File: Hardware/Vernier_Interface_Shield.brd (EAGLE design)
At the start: 91.4 x 71.1 mm, 37 parts, among them U1 74HC4052SO, U2 LMV358

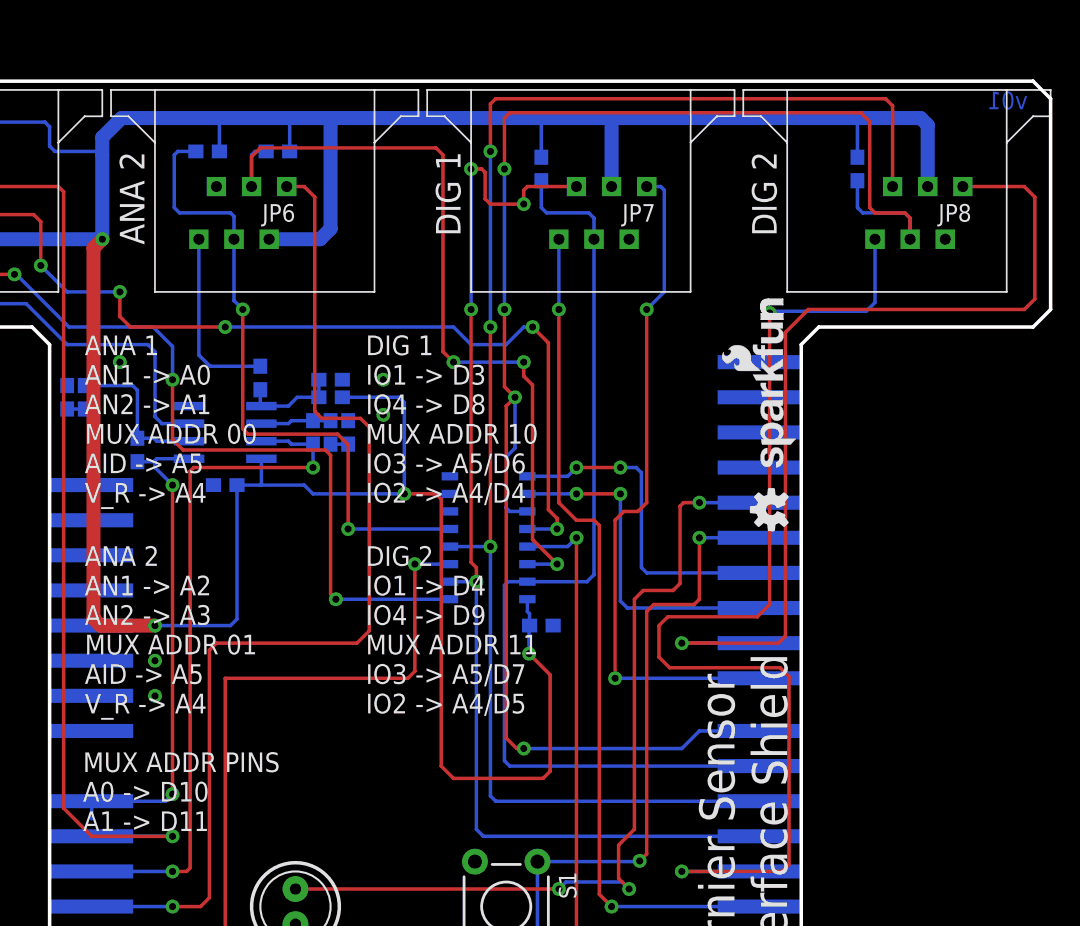
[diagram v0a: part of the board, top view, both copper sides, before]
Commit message: Tweaks towards v02
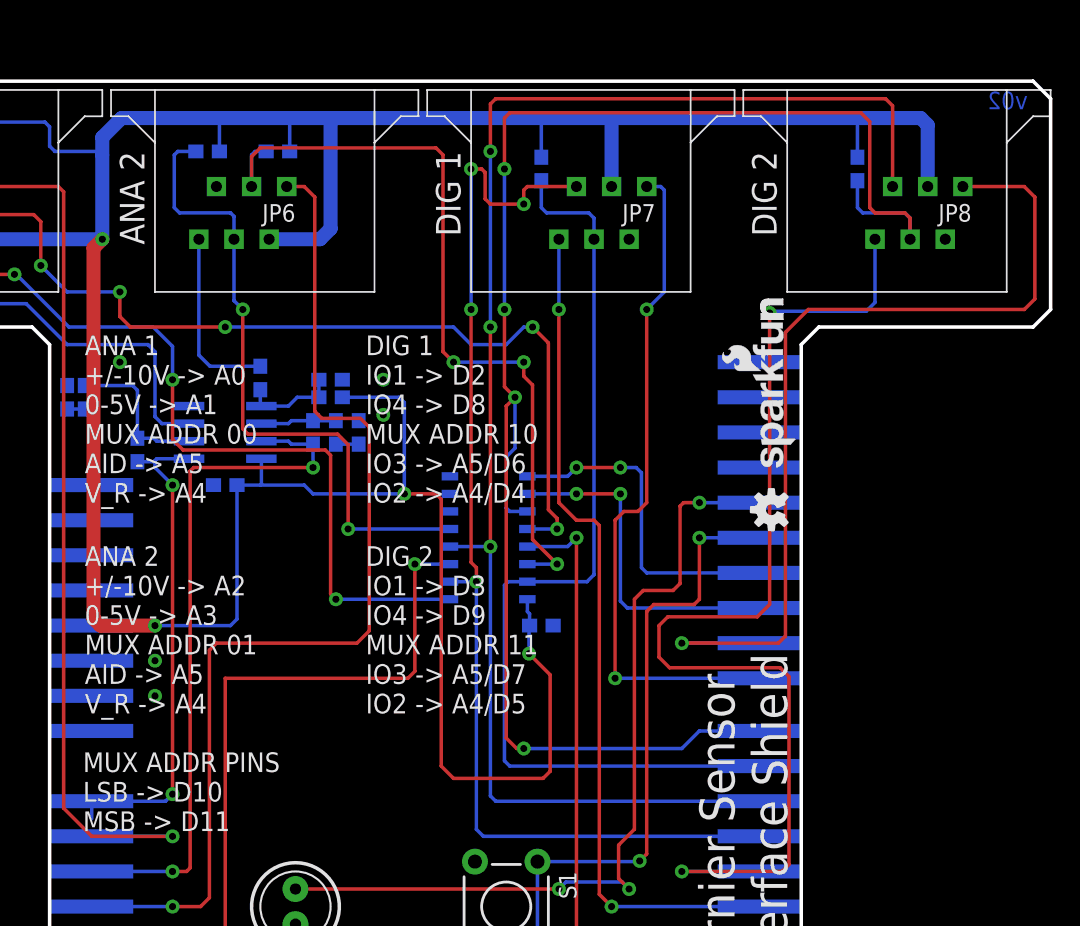
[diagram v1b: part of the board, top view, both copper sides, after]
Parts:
- moved R9 0.76 mm to (22.4, 45.7)
- moved R10 0.38 mm to (20.7, 45.7)
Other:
- board text added: "ANA 1 +/-10V -> A0 0-5V -> A1 MUX ADDR 00 AID -> A5 V_R -> A4"
- board text added: "ANA 2 +/-10V -> A2 0-5V -> A3 MUX ADDR 01 AID -> A5 V_R -> A4"
- board text added: "DIG 1 IO1 -> D2 IO4 -> D8 MUX ADDR 10 IO3 -> A5/D6 IO2 -> A4/D4"
- board text added: "DIG 2 IO1 -> D3 IO4 -> D9 MUX ADDR 11 IO3 -> A5/D7 IO2 -> A4/D5"
- board text added: "MUX ADDR PINS LSB -> D10 MSB -> D11"
- board text added: "v02"
- board text removed: "ANA 1 AN1 -> A0 AN2 -> A1 MUX ADDR 00 AID -> A5 V_R -> A4"
- board text removed: "ANA 2 AN1 -> A2 AN2 -> A3 MUX ADDR 01 AID -> A5 V_R -> A4"
- board text removed: "DIG 1 IO1 -> D3 IO4 -> D8 MUX ADDR 10 IO3 -> A5/D6 IO2 -> A4/D4"
- board text removed: "DIG 2 IO1 -> D4 IO4 -> D9 MUX ADDR 11 IO3 -> A5/D7 IO2 -> A4/D5"
- board text removed: "MUX ADDR PINS A0 -> D10 A1 -> D11"
- board text removed: "v01"
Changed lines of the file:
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@@
 <grid distance="0.05" unitdist="inch" unit="inch" style="lines" multiple="1" display="yes" altdistance="0.005" altunitdist="inch" altunit="inch"/>
 <layers>
-<layer number="1" name="Top" color="4" fill="1" visible="no" active="yes"/>
+<layer number="1" name="Top" color="4" fill="1" visible="yes" active="yes"/>
 <layer number="2" name="Route2" color="1" fill="3" visible="no" active="yes"/>
 <layer number="15" name="Route15" color="4" fill="6" visible="no" active="yes"/>
@@
 <layer number="19" name="Unrouted" color="6" fill="1" visible="yes" active="yes"/>
 <layer number="20" name="Dimension" color="6" fill="1" visible="yes" active="yes"/>
-<layer number="21" name="tPlace" color="16" fill="1" visible="no" active="yes"/>
+<layer number="21" name="tPlace" color="16" fill="1" visible="yes" active="yes"/>
 <layer number="22" name="bPlace" color="14" fill="1" visible="yes" active="yes"/>
-<layer number="23" name="tOrigins" color="15" fill="1" visible="no" active="yes"/>
+<layer number="23" name="tOrigins" color="15" fill="1" visible="yes" active="yes"/>
 <layer number="24" name="bOrigins" color="15" fill="1" visible="yes" active="yes"/>
 <layer number="25" name="tNames" color="7" fill="1" visible="no" active="yes"/>
@@
 <layer number="41" name="tRestrict" color="4" fill="10" visible="no" active="yes"/>
 <layer number="42" name="bRestrict" color="1" fill="10" visible="no" active="yes"/>
+<layer number="43" name="vRestrict" color="2" fill="10" visible="no" active="yes"/>
 <layer number="44" name="Drills" color="7" fill="1" visible="no" active="yes"/>
-<layer number="45" name="Holes" color="7" fill="1" visible="no" active="yes"/>
+<layer number="45" name="Holes" color="7" fill="1" visible="yes" active="yes"/>
 <layer number="46" name="Milling" color="3" fill="1" visible="no" active="yes"/>
-<layer number="51" name="tDocu" color="6" fill="1" visible="no" active="yes"/>
+<layer number="51" name="tDocu" color="6" fill="1" visible="yes" active="yes"/>
 <layer number="52" name="bDocu" color="7" fill="1" visible="no" active="yes"/>
 <layer number="3" name="Route3" color="4" fill="3" visible="no" active="no"/>
@@
 <layer number="37" name="tTest" color="7" fill="1" visible="no" active="no"/>
 <layer number="38" name="bTest" color="7" fill="1" visible="no" active="no"/>
-<layer number="43" name="vRestrict" color="2" fill="10" visible="no" active="no"/>
 <layer number="47" name="Measures" color="7" fill="1" visible="no" active="no"/>
 <layer number="48" name="Document" color="7" fill="1" visible="no" active="no"/>
@@
 <layer number="106" name="bPlate" color="7" fill="1" visible="no" active="no"/>
 <layer number="107" name="Crop" color="7" fill="1" visible="no" active="no"/>
-<layer number="108" name="tplace-old" color="10" fill="1" visible="no" active="yes"/>
-<layer number="109" name="ref-old" color="11" fill="1" visible="no" active="yes"/>
+<layer number="108" name="tplace-old" color="10" fill="1" visible="no" active="no"/>
+<layer number="109" name="ref-old" color="11" fill="1" visible="no" active="no"/>
 <layer number="116" name="Patch_BOT" color="9" fill="4" visible="no" active="no"/>
 <layer number="121" name="_tsilk" color="7" fill="1" visible="no" active="no"/>
@@
 <layer number="144" name="Drill_legend" color="7" fill="1" visible="no" active="no"/>
 <layer number="151" name="HeatSink" color="7" fill="1" visible="no" active="no"/>
-<layer number="199" name="Contour" color="7" fill="1" visible="no" active="yes"/>
+<layer number="199" name="Contour" color="7" fill="1" visible="no" active="no"/>
 <layer number="200" name="200bmp" color="1" fill="10" visible="no" active="no"/>
 <layer number="201" name="201bmp" color="2" fill="10" visible="no" active="no"/>
@@
 <text x="48.006" y="48.26" size="1.27" layer="22" font="vector" ratio="15" rot="SMR0" align="center-left">SDA</text>
 <text x="48.006" y="50.8" size="1.27" layer="22" font="vector" ratio="15" rot="SMR0" align="center-left">SCL</text>
-<text x="70.739" y="69.723" size="1.27" layer="16" font="vector" ratio="20" rot="SMR0" align="center-left">v01</text>
+<text x="70.739" y="69.723" size="1.27" layer="16" font="vector" ratio="20" rot="SMR0" align="center-left">v02</text>
 <wire x1="35.56" y1="46.99" x2="27.94" y2="46.99" width="0.508" layer="30"/>
 <wire x1="25.4" y1="46.99" x2="17.78" y2="46.99" width="0.508" layer="30"/>
@@
 <text x="17.78" y="5.08" size="1.778" layer="21" font="vector" ratio="15" align="bottom-center">D13</text>
 <text x="2.54" y="40.64" size="1.4224" layer="21" font="vector" ratio="15">ANA 1
-AN1 -&gt; A0
-AN2 -&gt; A1
++/-10V -&gt; A0
+0-5V -&gt; A1
 MUX ADDR 00
 AID -&gt; A5
 V_R -&gt; A4</text>
 <text x="2.54" y="25.4" size="1.4224" layer="21" font="vector" ratio="15">ANA 2
-AN1 -&gt; A2
-AN2 -&gt; A3
++/-10V -&gt; A2
+0-5V -&gt; A3
 MUX ADDR 01
 AID -&gt; A5
 V_R -&gt; A4</text>
 <text x="22.86" y="40.64" size="1.4224" layer="21" font="vector" ratio="15">DIG 1
-IO1 -&gt; D3
+IO1 -&gt; D2
 IO4 -&gt; D8
 MUX ADDR 10
@@
 IO2 -&gt; A4/D4</text>
 <text x="22.86" y="25.4" size="1.4224" layer="21" font="vector" ratio="15">DIG 2
-IO1 -&gt; D4
+IO1 -&gt; D3
 IO4 -&gt; D9
 MUX ADDR 11
@@
 <text x="16.51" y="93.98" size="2.54" layer="25" font="vector" ratio="15">M. Hord</text>
 <text x="2.413" y="16.891" size="1.4224" layer="21" font="vector" ratio="15">MUX ADDR PINS
-A0 -&gt; D10
-A1 -&gt; D11</text>
+LSB -&gt; D10
+MSB -&gt; D11</text>
 </plain>
 <attributes>
@@
 <attribute name="PROD_ID" value="RES-09383" x="19.05" y="53.467" size="1.778" layer="28" font="vector" ratio="15" rot="MR270" display="off"/>
 </element>
-<element name="R9" library="SparkFun-Resistors" package="0603-RES" value="20k" x="21.59" y="45.72" rot="MR270">
-<attribute name="PROD_ID" value="RES-09383" x="25.4" y="45.72" size="1.778" layer="28" font="vector" ratio="15" rot="MR270" display="off"/>
-</element>
-<element name="R10" library="SparkFun-Resistors" package="0603-RES" value="20k" x="20.32" y="45.72" rot="MR90">
-<attribute name="PROD_ID" value="RES-09383" x="12.7" y="41.91" size="1.778" layer="28" font="vector" ratio="15" rot="MR90" display="off"/>
+<element name="R9" library="SparkFun-Resistors" package="0603-RES" value="20k" x="22.352" y="45.72" rot="MR270">
+<attribute name="PROD_ID" value="RES-09383" x="26.162" y="45.72" size="1.778" layer="28" font="vector" ratio="15" rot="MR270" display="off"/>
+</element>
+<element name="R10" library="SparkFun-Resistors" package="0603-RES" value="20k" x="20.701" y="45.72" rot="MR90">
+<attribute name="PROD_ID" value="RES-09383" x="13.081" y="41.91" size="1.778" layer="28" font="vector" ratio="15" rot="MR90" display="off"/>
 </element>
 <element name="R11" library="SparkFun-Resistors" package="0603-RES" value="10K" x="19.05" y="45.72" rot="MR270">
@@
 <contactref element="R9" pad="2"/>
 <contactref element="R10" pad="1"/>
-<wire x1="21.59" y1="44.87" x2="20.32" y2="44.87" width="0.254" layer="16"/>
+<wire x1="22.352" y1="44.87" x2="20.701" y2="44.87" width="0.254" layer="16"/>
 </signal>
 <signal name="N$6">
@@
 <contactref element="R11" pad="1"/>
 <contactref element="U2" pad="6"/>
-<wire x1="20.32" y1="46.57" x2="19.05" y2="46.57" width="0.254" layer="16"/>
+<wire x1="20.701" y1="46.57" x2="19.05" y2="46.57" width="0.254" layer="16"/>
 <wire x1="19.05" y1="46.57" x2="17.487" y2="46.57" width="0.254" layer="16"/>
 <wire x1="17.487" y1="46.57" x2="17.272" y2="46.355" width="0.254" layer="16"/>
@@
 </signal>
 </signals>
-<errors>
-</errors>
 </board>
 </drawing>

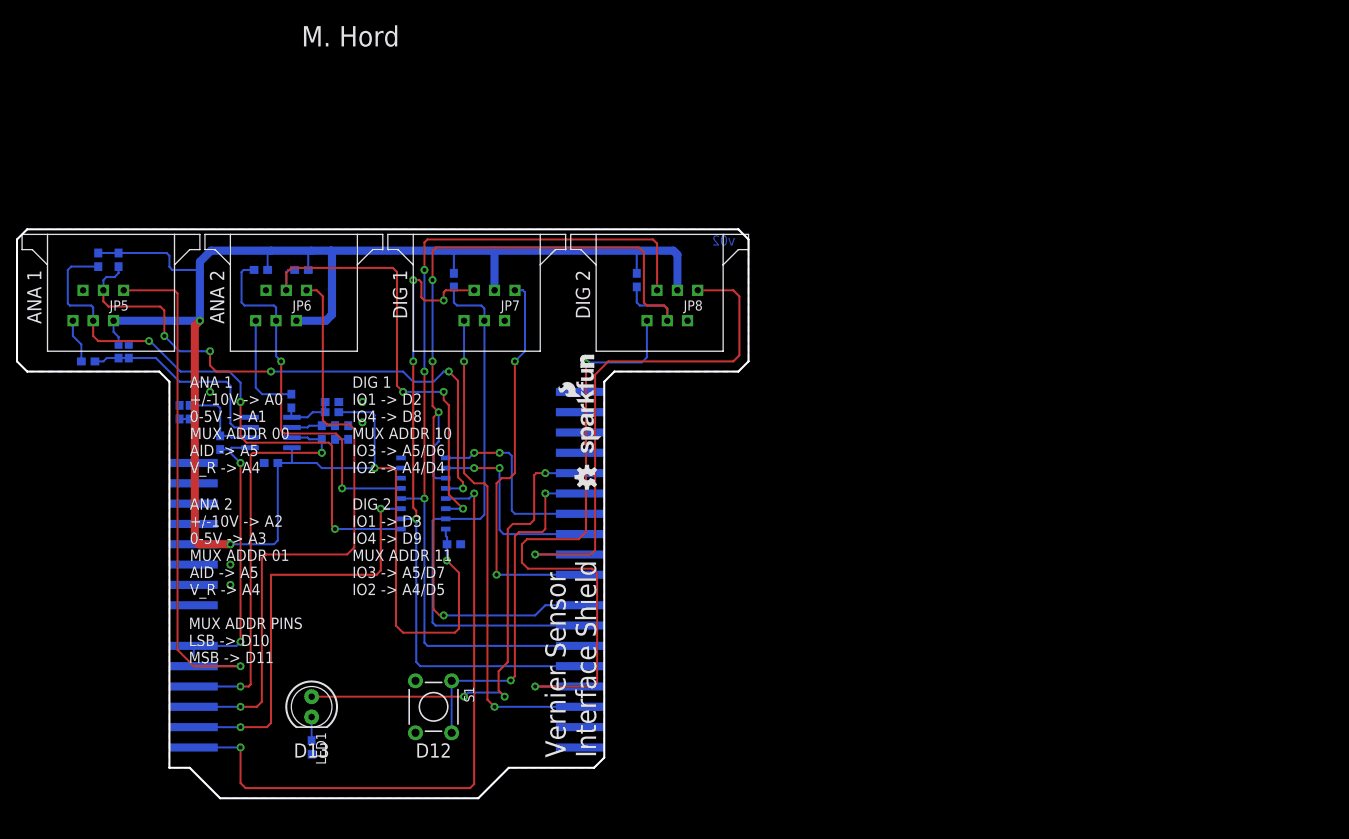
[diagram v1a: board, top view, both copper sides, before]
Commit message: Updated footprints of BTA and BTD
Fixed the footprints of BTA and BTD.
Corrected the BTD pin numbering.
Rotated the design so that the connectors don't short out on the USB
cage.
V03
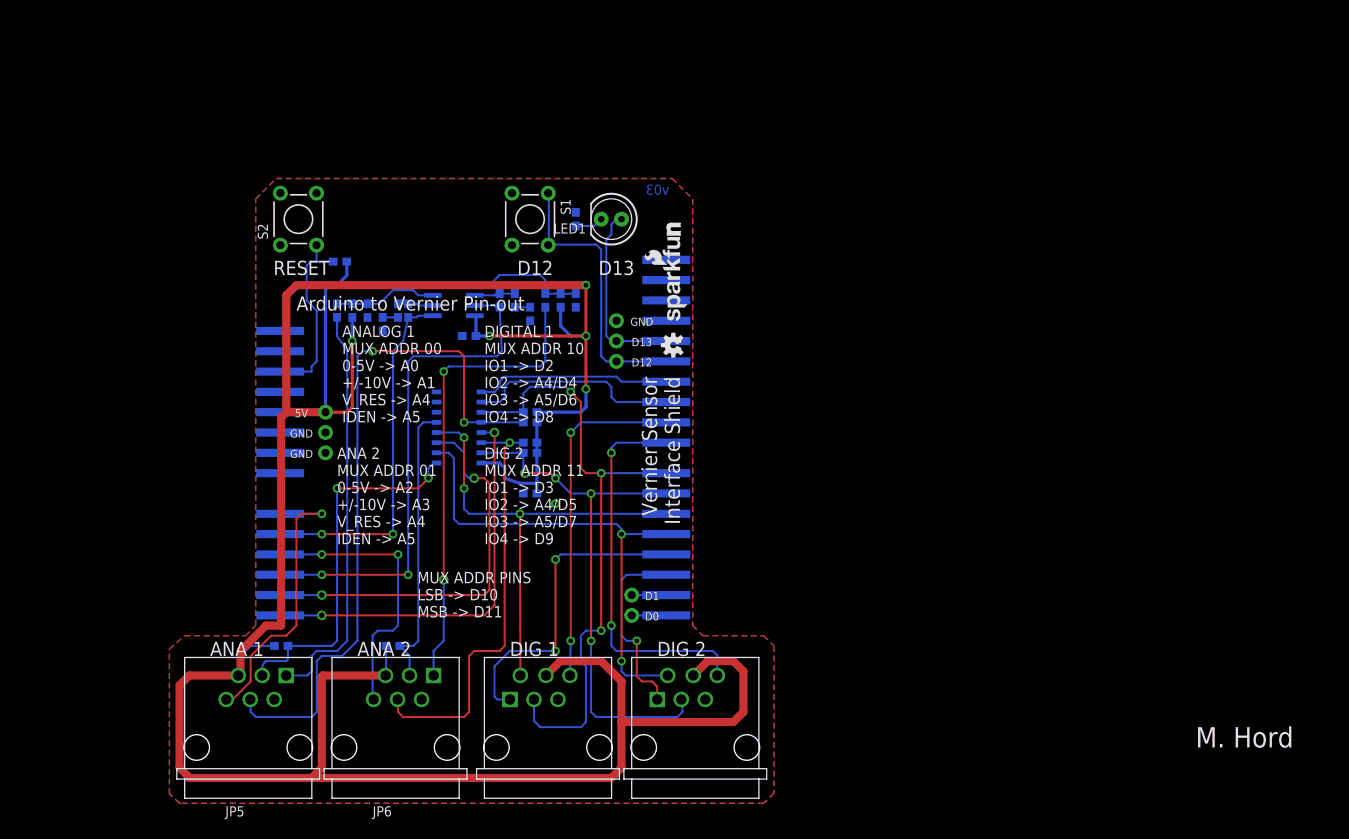
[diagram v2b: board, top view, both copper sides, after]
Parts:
- added R20: 10K, SparkFun-Resistors:0603-RES
- added S2: (no value), SparkFun-Electromechanical:TACTILE-PTH
- moved FRAME1 150.6 mm to (109.6, 10.2)
- moved R19 73.8 mm to (50.8, 72.4), turned to 270 degrees
- moved LED1 71.6 mm to (55.2, 72.4), turned to 180 degrees
- moved JP7 62.2 mm to (57.8, 0.00), turned to 0 degrees
- moved S1 62.1 mm to (45.1, 72.4)
- moved JP5 58.5 mm to (1.91, 0.00), turned to 0 degrees
- moved JP8 57.6 mm to (39.4, 0.00), turned to 0 degrees
- moved JP6 57.3 mm to (20.3, 0.00), turned to 0 degrees
- moved R13 55.3 mm to (45.1, 47.0), turned to 0 degrees
- moved R14 53.4 mm to (14.0, 19.1), turned to 180 degrees
- moved R16 49.8 mm to (27.9, 19.1), turned to 180 degrees
- moved R15 35.8 mm to (45.1, 44.5)
- moved R8 34.1 mm to (47.0, 62.2), turned to 90 degrees
- moved R7 33.0 mm to (50.8, 62.2), turned to 90 degrees
- moved R12 31.8 mm to (48.9, 62.2), turned to 270 degrees
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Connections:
- removed net A0: JP4.6, R5.2, U2.1
- removed net A2: JP4.4, R11.2, U2.7
- new net A1: JP4.5, R5.2, U2.1
- new net A3: JP4.3, R11.2, U2.7
- net 5V: now also R20.2
- net AS1_AN2: now also JP4.6; no longer JP4.5
- net AS2_AN2: now also JP4.4; no longer JP4.3
- net GND: now also S2.1
- net RESET: now also R20.1, S2.3
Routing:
- net 5V: track 251.4 -> 355.3 mm, vias 4 -> 6
- net A3: track 0.00 -> 64.2 mm, vias 0 -> 2
- net A2: track 50.4 -> 0.00 mm, vias 2 -> 0
- net D2_IO2: track 107.8 -> 58.4 mm
- net AS1_AN1: track 5.52 -> 51.3 mm
- net AS2_AN1: track 13.2 -> 58.5 mm, vias 0 -> 2
- net A1: track 0.00 -> 45.0 mm, vias 0 -> 2
- net D2_IO1: track 81.6 -> 39.8 mm
- net D2_IO3: track 119.9 -> 78.4 mm, vias 4 -> 3
- net AS2_AN2: track 75.8 -> 35.3 mm, vias 1 -> 2
- net 13: track 61.5 -> 23.5 mm, vias 3 -> 1
- net D1_IO1: track 61.3 -> 24.1 mm, vias 2 -> 1
- net A0: track 35.8 -> 0.00 mm, vias 2 -> 0
- net AS1_AN2: track 66.5 -> 36.4 mm
- net A5: track 80.6 -> 50.6 mm
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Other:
- board outline removed
- board text added: "ANA 2 MUX ADDR 01 0-5V -> A2 +/-10V -> A3 V_RES -> A4 IDEN -> A5"
- board text added: "ANALOG 1 MUX ADDR 00 0-5V -> A0 +/-10V -> A1 V_RES -> A4 IDEN -> A5"
- board text added: "Arduino to Vernier Pin-out"
- board text added: "DIG 2 MUX ADDR 11 IO1 -> D3 IO2 -> A4/D5 IO3 -> A5/D7 IO4 -> D9"
- board text added: "DIGITAL 1 MUX ADDR 10 IO1 -> D2 IO2 -> A4/D4 IO3 -> A5/D6 IO4 -> D8"
- board text added: "RESET"
- board text added: "v03"
- board text removed: "ANA 1 +/-10V -> A0 0-5V -> A1 MUX ADDR 00 AID -> A5 V_R -> A4"
- board text removed: "ANA 2 +/-10V -> A2 0-5V -> A3 MUX ADDR 01 AID -> A5 V_R -> A4"
- board text removed: "DIG 1 IO1 -> D2 IO4 -> D8 MUX ADDR 10 IO3 -> A5/D6 IO2 -> A4/D4"
- board text removed: "DIG 2 IO1 -> D3 IO4 -> D9 MUX ADDR 11 IO3 -> A5/D7 IO2 -> A4/D5"
- board text removed: "v02"

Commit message: Fixed traces, ran DRC, etc...
Updated traces, fixed errors in DRC... more tweaks toward v02
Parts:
- added JP10, JP9: (no value), SparkFun-Connectors:1X03_NO_SILK
- added JP11: M021X02_NO_SILK, SparkFun-Connectors:1X02_NO_SILK
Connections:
- net 0: now also JP11.2
- net 1: now also JP11.1
- net 12: now also JP10.1
- net 13: now also JP10.2
- net 5V: now also JP9.1
- net GND: now also JP10.3, JP9.2, JP9.3
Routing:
- net 5V: track 355.3 -> 345.7 mm, vias 6 -> 4
- net 13: track 23.5 -> 24.8 mm, vias 1 -> 0
- net 12: vias 1 -> 0
- net 1: vias 1 -> 0
- net 0: vias 1 -> 0
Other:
- board text added: "v02"
- board text removed: "v03"
